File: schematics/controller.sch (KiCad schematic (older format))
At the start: 21 parts

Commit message: updated controller schematic
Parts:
- removed BT?: Battery_Cell, symbol Device:Battery_Cell
- removed C?: 100nF, symbol Device:C
- removed P?: USB_C_Plug_USB2.0, symbol Connector:USB_C_Plug_USB2.0
- removed Q? (x2): BSN20, Package_TO_SOT_SMD:SOT-23, symbol Transistor_FET:BSN20
- removed R?: 330, symbol Device:R
- removed R?: 2.7k, symbol Device:R
- removed R?: 5k, symbol Device:R
- removed U?: AP9101CK6, Package_TO_SOT_SMD:SOT-23-6, symbol Battery_Management:AP9101CK6
- added C1, C2: 100nF, symbol Device:C
- added J1: Conn_01x02, symbol Connector_Generic:Conn_01x02
- added J2: Conn_01x06, symbol Connector_Generic:Conn_01x06
- added J3: Conn_01x09, symbol Connector_Generic:Conn_01x09
- added R1, R2: 10k, symbol Device:R
- added SW1, SW2: SW_Push, symbol Switch:SW_Push
- gave numbers to parts that had none: 12
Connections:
- net labels added: 5V, CTS, DTR, IO25, IO26, IO27, IO32, IO33, IO34, IO35, RX, TX, Vcc
- net labels removed: +3V3, P+, P-
- wire segments 74 -> 58
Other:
- note added: "Battery charger connections"
- note added: "Boot pin"
- note added: "Extra Connectors\n"
- note added: "Inputs"
- note added: "Linear regulator\n"
- note added: "Reset pin\n"
- note added: "UART connectors\n"
- moved on the sheet: R3, R4, R5, R6, R7, SW3, SW4, SW5, SW6, SW7, U1

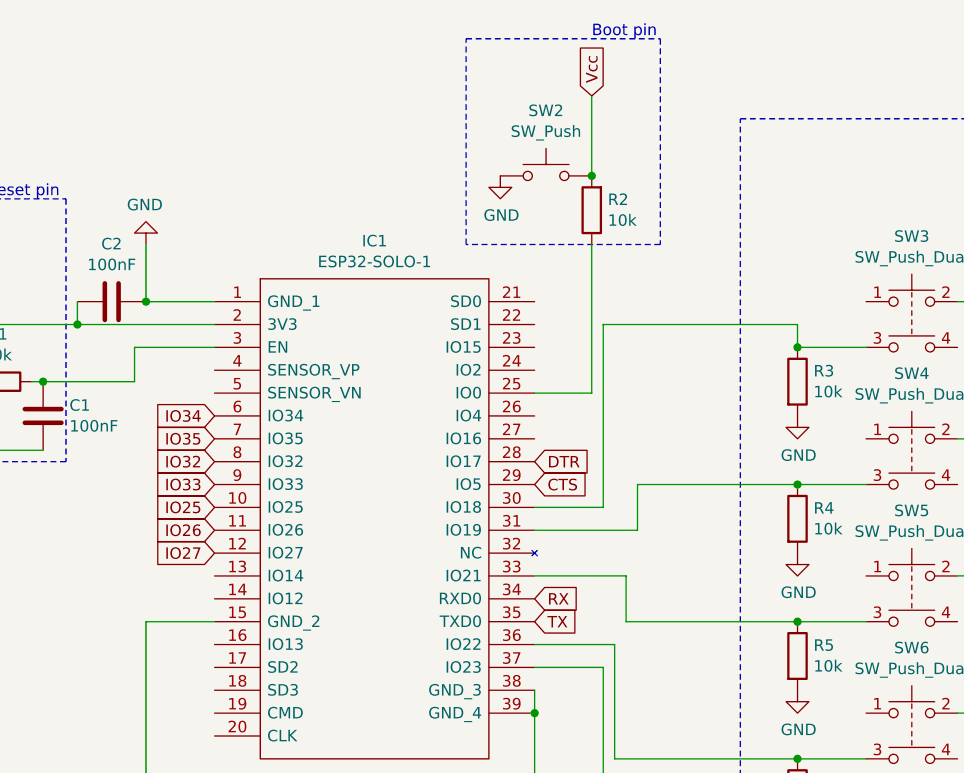
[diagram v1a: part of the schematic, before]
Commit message: added drivers for display
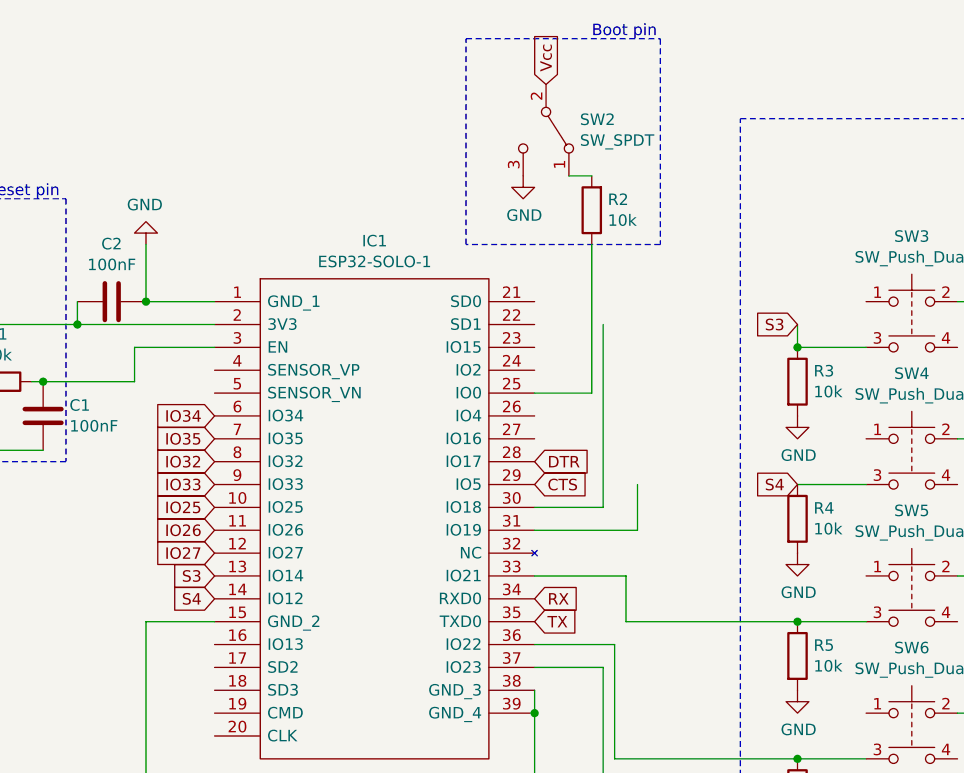
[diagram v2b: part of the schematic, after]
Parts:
- removed SW2: SW_Push, symbol Switch:SW_Push
- added SW2: SW_SPDT, Button_Switch_THT:SW_Slide_1P2T_CK_OS102011MS2Q, symbol Switch:SW_SPDT
- C1, C2: footprint (none) -> Capacitor_SMD:C_0805_2012Metric
- IC1: footprint ESP32SOLO1 -> RF_Module:ESP32-WROOM-32
- J1: footprint (none) -> Connector_PinHeader_1.00mm:PinHeader_1x02_P1.00mm_Vertical
- J2: footprint (none) -> Connector_PinSocket_1.00mm:PinSocket_1x06_P1.00mm_Vertical
- J3: footprint (none) -> Connector_PinSocket_1.00mm:PinSocket_1x09_P1.00mm_Vertical
- R1, R2, R3, R4, R5, R6, R7: footprint (none) -> Resistor_SMD:R_0805_2012Metric
- SW1, SW3, SW4, SW5, SW6, SW7: footprint (none) -> Button_Switch_THT:SW_TH_Tactile_Omron_B3F-10xx
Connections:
- net labels added: S3, S4
- wire segments 58 -> 56
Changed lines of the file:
@@
 F 0 "IC1" H 7400 1965 50  0000 C CNN
 F 1 "ESP32-SOLO-1" H 7400 1874 50  0000 C CNN
-F 2 "ESP32SOLO1" H 7950 1800 50  0001 L CNN
+F 2 "RF_Module:ESP32-WROOM-32" H 7950 1800 50  0001 L CNN
 F 3 "https://www.espressif.com/sites/default/files/documentation/esp32-solo-1_datasheet_en.pdf" H 7950 1700 50  0001 L CNN
 F 4 "WiFi Modules (802.11) SMD Module, ESP32-S0WD, 32Mbits SPI flash, UART mode," H 7950 1600 50  0001 L CNN "Description"
@@
 F 0 "SW3" H 9750 1985 50  0000 C CNN
 F 1 "SW_Push_Dual" H 9750 1894 50  0000 C CNN
-F 2 "" H 9750 1900 50  0001 C CNN
+F 2 "Button_Switch_THT:SW_TH_Tactile_Omron_B3F-10xx" H 9750 1900 50  0001 C CNN
 F 3 "~" H 9750 1900 50  0001 C CNN
 	1    9750 1700
@@
 F 0 "SW4" H 9750 2585 50  0000 C CNN
 F 1 "SW_Push_Dual" H 9750 2494 50  0000 C CNN
-F 2 "" H 9750 2500 50  0001 C CNN
+F 2 "Button_Switch_THT:SW_TH_Tactile_Omron_B3F-10xx" H 9750 2500 50  0001 C CNN
 F 3 "~" H 9750 2500 50  0001 C CNN
 	1    9750 2300
@@
 F 0 "SW5" H 9750 3185 50  0000 C CNN
 F 1 "SW_Push_Dual" H 9750 3094 50  0000 C CNN
-F 2 "" H 9750 3100 50  0001 C CNN
+F 2 "Button_Switch_THT:SW_TH_Tactile_Omron_B3F-10xx" H 9750 3100 50  0001 C CNN
 F 3 "~" H 9750 3100 50  0001 C CNN
 	1    9750 2900
@@
 F 0 "SW6" H 9750 3785 50  0000 C CNN
 F 1 "SW_Push_Dual" H 9750 3694 50  0000 C CNN
-F 2 "" H 9750 3700 50  0001 C CNN
+F 2 "Button_Switch_THT:SW_TH_Tactile_Omron_B3F-10xx" H 9750 3700 50  0001 C CNN
 F 3 "~" H 9750 3700 50  0001 C CNN
 	1    9750 3500
@@
 F 0 "SW7" H 9750 4385 50  0000 C CNN
 F 1 "SW_Push_Dual" H 9750 4294 50  0000 C CNN
-F 2 "" H 9750 4300 50  0001 C CNN
+F 2 "Button_Switch_THT:SW_TH_Tactile_Omron_B3F-10xx" H 9750 4300 50  0001 C CNN
 F 3 "~" H 9750 4300 50  0001 C CNN
 	1    9750 4100
@@
 F 0 "R3" H 9320 2096 50  0000 L CNN
 F 1 "10k" H 9320 2005 50  0000 L CNN
-F 2 "" V 9180 2050 50  0001 C CNN
+F 2 "Resistor_SMD:R_0805_2012Metric" V 9180 2050 50  0001 C CNN
 F 3 "~" H 9250 2050 50  0001 C CNN
 	1    9250 2050
@@
 F 0 "R4" H 9320 2696 50  0000 L CNN
 F 1 "10k" H 9320 2605 50  0000 L CNN
-F 2 "" V 9180 2650 50  0001 C CNN
+F 2 "Resistor_SMD:R_0805_2012Metric" V 9180 2650 50  0001 C CNN
 F 3 "~" H 9250 2650 50  0001 C CNN
 	1    9250 2650
@@
 F 0 "R5" H 9320 3296 50  0000 L CNN
 F 1 "10k" H 9320 3205 50  0000 L CNN
-F 2 "" V 9180 3250 50  0001 C CNN
+F 2 "Resistor_SMD:R_0805_2012Metric" V 9180 3250 50  0001 C CNN
 F 3 "~" H 9250 3250 50  0001 C CNN
 	1    9250 3250
@@
 F 0 "R6" H 9320 3896 50  0000 L CNN
 F 1 "10k" H 9320 3805 50  0000 L CNN
-F 2 "" V 9180 3850 50  0001 C CNN
+F 2 "Resistor_SMD:R_0805_2012Metric" V 9180 3850 50  0001 C CNN
 F 3 "~" H 9250 3850 50  0001 C CNN
 	1    9250 3850
@@
 F 0 "R7" H 9320 4496 50  0000 L CNN
 F 1 "10k" H 9320 4405 50  0000 L CNN
-F 2 "" V 9180 4450 50  0001 C CNN
+F 2 "Resistor_SMD:R_0805_2012Metric" V 9180 4450 50  0001 C CNN
 F 3 "~" H 9250 4450 50  0001 C CNN
 	1    9250 4450
@@
 Wire Wire Line
 	9550 2500 9250 2500
-Connection ~ 9250 2500
 Wire Wire Line
 	9550 3100 9250 3100
@@
 F 0 "C2" V 5998 1700 50  0000 C CNN
 F 1 "100nF" V 6089 1700 50  0000 C CNN
-F 2 "" H 6288 1550 50  0001 C CNN
+F 2 "Capacitor_SMD:C_0805_2012Metric" H 6288 1550 50  0001 C CNN
 F 3 "~" H 6250 1700 50  0001 C CNN
 	1    6250 1700
@@
 F 0 "J3" V 3925 3296 50  0000 C CNN
 F 1 "Conn_01x09" V 4016 3296 50  0000 C CNN
-F 2 "" H 3800 3300 50  0001 C CNN
+F 2 "Connector_PinSocket_1.00mm:PinSocket_1x09_P1.00mm_Vertical" H 3800 3300 50  0001 C CNN
 F 3 "~" H 3800 3300 50  0001 C CNN
 	1    3800 3300
@@
 F 0 "J1" V 1622 2530 50  0000 L CNN
 F 1 "Conn_01x02" V 1713 2530 50  0000 L CNN
-F 2 "" H 1750 2450 50  0001 C CNN
+F 2 "Connector_PinHeader_1.00mm:PinHeader_1x02_P1.00mm_Vertical" H 1750 2450 50  0001 C CNN
 F 3 "~" H 1750 2450 50  0001 C CNN
 	1    1750 2450
@@
 F 0 "R1" V 5543 2050 50  0000 C CNN
 F 1 "10k" V 5634 2050 50  0000 C CNN
-F 2 "" V 5680 2050 50  0001 C CNN
+F 2 "Resistor_SMD:R_0805_2012Metric" V 5680 2050 50  0001 C CNN
 F 3 "~" H 5750 2050 50  0001 C CNN
 	1    5750 2050
@@
 F 0 "SW1" H 5250 2335 50  0000 C CNN
 F 1 "SW_Push" H 5250 2244 50  0000 C CNN
-F 2 "" H 5250 2250 50  0001 C CNN
+F 2 "Button_Switch_THT:SW_TH_Tactile_Omron_B3F-10xx" H 5250 2250 50  0001 C CNN
 F 3 "~" H 5250 2250 50  0001 C CNN
 	1    5250 2050
@@
 F 0 "R2" H 8280 1254 50  0000 R CNN
 F 1 "10k" H 8280 1345 50  0000 R CNN
-F 2 "" V 8280 1300 50  0001 C CNN
+F 2 "Resistor_SMD:R_0805_2012Metric" V 8280 1300 50  0001 C CNN
 F 3 "~" H 8350 1300 50  0001 C CNN
 	1    8350 1300
@@
 	8100 2100 8350 2100
 $Comp
-L Switch:SW_Push SW2
-U 1 1 62125195
-P 8150 1150
-F 0 "SW2" H 8150 1435 50  0000 C CNN
-F 1 "SW_Push" H 8150 1344 50  0000 C CNN
-F 2 "" H 8150 1350 50  0001 C CNN
-F 3 "~" H 8150 1350 50  0001 C CNN
-	1    8150 1150
-	1    0    0    -1
-$EndComp
-$Comp
 L power:GND #PWR08
 U 1 1 621259D0
-P 7950 1150
-F 0 "#PWR08" H 7950 900 50  0001 C CNN
-F 1 "GND" H 7955 977 50  0000 C CNN
-F 2 "" H 7950 1150 50  0001 C CNN
-F 3 "" H 7950 1150 50  0001 C CNN
-	1    7950 1150
-	1    0    0    -1
-$EndComp
-Text GLabel 8350 800  1    50   Input ~ 0
+P 8050 1150
+F 0 "#PWR08" H 8050 900 50  0001 C CNN
+F 1 "GND" H 8055 977 50  0000 C CNN
+F 2 "" H 8050 1150 50  0001 C CNN
+F 3 "" H 8050 1150 50  0001 C CNN
+	1    8050 1150
+	1    0    0    -1
+$EndComp
+Text GLabel 8150 750  1    50   Input ~ 0
 Vcc
-Wire Wire Line
-	8350 800  8350 1150
-Connection ~ 8350 1150
 Wire Wire Line
 	5450 1800 6100 1800
@@
 F 0 "J2" V 3622 4930 50  0000 L CNN
 F 1 "Conn_01x06" V 3713 4930 50  0000 L CNN
-F 2 "" H 3750 4650 50  0001 C CNN
+F 2 "Connector_PinSocket_1.00mm:PinSocket_1x06_P1.00mm_Vertical" H 3750 4650 50  0001 C CNN
 F 3 "~" H 3750 4650 50  0001 C CNN
 	1    3750 4650
@@
 F 0 "C1" H 5835 2154 50  0000 R CNN
 F 1 "100nF" H 5835 2245 50  0000 R CNN
-F 2 "" H 5988 2050 50  0001 C CNN
+F 2 "Capacitor_SMD:C_0805_2012Metric" H 5988 2050 50  0001 C CNN
 F 3 "~" H 5950 2200 50  0001 C CNN
 	1    5950 2200
@@
 Connection ~ 5050 2200
 Wire Wire Line
-	8400 1800 9250 1800
-Wire Wire Line
-	8550 2500 9250 2500
-Wire Wire Line
 	8500 3100 9250 3100
 Wire Wire Line
@@
 Text Notes 10800 900  0    50   ~ 0
 Inputs
+$Comp
+L Switch:SW_SPDT SW2
+U 1 1 62171098
+P 8150 950
+F 0 "SW2" V 8104 1098 50  0000 L CNN
+F 1 "SW_SPDT" V 8195 1098 50  0000 L CNN
+F 2 "Button_Switch_THT:SW_Slide_1P2T_CK_OS102011MS2Q" H 8150 950 50  0001 C CNN
+F 3 "~" H 8150 950 50  0001 C CNN
+	1    8150 950
+	0    1    1    0
+$EndComp
+Wire Wire Line
+	8350 1150 8250 1150
+Text GLabel 9250 2500 0    50   Input ~ 0
+S4
+Text GLabel 9250 1800 0    50   Input ~ 0
+S3
+Text GLabel 6700 2900 0    50   Input ~ 0
+S3
+Text GLabel 6700 3000 0    50   Input ~ 0
+S4
 $EndSCHEMATC

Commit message: finished (I think) schematics for tower and controller
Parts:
- removed IC1: ESP32-SOLO-1, RF_Module:ESP32-WROOM-32, symbol controller-rescue:ESP32-SOLO-1-ESP-SOLO-1
- removed J1: Conn_01x02, Connector_PinHeader_1.00mm:PinHeader_1x02_P1.00mm_Vertical, symbol Connector_Generic:Conn_01x02
- removed J3: Conn_01x09, Connector_PinSocket_1.00mm:PinSocket_1x09_P1.00mm_Vertical, symbol Connector_Generic:Conn_01x09
- removed SW2: SW_SPDT, Button_Switch_THT:SW_Slide_1P2T_CK_OS102011MS2Q, symbol Switch:SW_SPDT
- removed U1: NCP1117-3.3_SOT223, Package_TO_SOT_SMD:SOT-223-3_TabPin2, symbol Regulator_Linear:NCP1117-3.3_SOT223
- added C3, C5: 100nF, Capacitor_SMD:C_0805_2012Metric, symbol Device:C
- added C4: 22uF, Capacitor_SMD:C_0805_2012Metric, symbol Device:C
- added D1: LED, Mouser:APHCM2012QBCDF01, symbol Device:LED
- added IC1: AZ1117CD-3.3TRG1, Mouser:AZ1117CD33TRG1, symbol Mouser:AZ1117CD-3.3TRG1
- added IC2: ESP32-SOLO-1, Mouser:ESP32SOLO1, symbol ESP-SOLO-1:ESP32-SOLO-1
- added J1, J2: Conn_01x05, Connector_PinSocket_2.54mm:PinSocket_1x05_P2.54mm_Vertical, symbol Connector_Generic:Conn_01x05
- added Q1, Q2: SS8050-G, Mouser:SOT95P240X115-3N, symbol Mouser:SS8050-G
- added R8: 10k, Resistor_SMD:R_0805_2012Metric, symbol Device:R
- added R9: 0, Resistor_SMD:R_0805_2012Metric, symbol Device:R
- added SW2: SW_Push, Button_Switch_SMD:SW_SPST_CK_KXT3, symbol Switch:SW_Push
- C1, C2: value 100nF -> 0.1uF
- J3: renamed from J2; footprint Connector_PinSocket_1.00mm:PinSocket_1x06_P1.00mm_Vertical -> Connector_PinSocket_2.54mm:PinSocket_1x06_P2.54mm_Vertical
- SW1: footprint Button_Switch_THT:SW_TH_Tactile_Omron_B3F-10xx -> Button_Switch_SMD:SW_SPST_CK_KXT3
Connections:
- net labels added: 5v, BAT, Dn, Dp, EN, GPIO0, GPIO13, GPIO22, GPIO23, S1, S2, S5
- net labels removed: 5V, IO25, IO26, IO27, IO32, IO33, IO34, IO35
- wire segments 56 -> 61
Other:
- note added: "Battery charger"
- note added: "Boot PushButton"
- note added: "Control buttons"
- note added: "ESP32 module"
- note added: "Extra connectors"
- note added: "Linear Regulator\n"
- note added: "MCU Power Capacitors"
- note added: "Power LED"
- note added: "Program circuitry\n"
- note added: "Reset PushButton"
- note added: "Reset Stabilizing"
- note removed: "Battery charger connections"
- note removed: "Boot pin"
- note removed: "Extra Connectors\n"
- note removed: "Inputs"
- note removed: "Linear regulator\n"
- note removed: "Reset pin\n"
- moved on the sheet: J3
